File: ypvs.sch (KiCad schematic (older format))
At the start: 21 parts, among them J1 Servo, J2 LM_2596 _Input, J3 HV_Cable, J4 Motorcycle Battery, U1 Stm32f103_BluePill, U2 LM1117-3.3, U3 H11L1

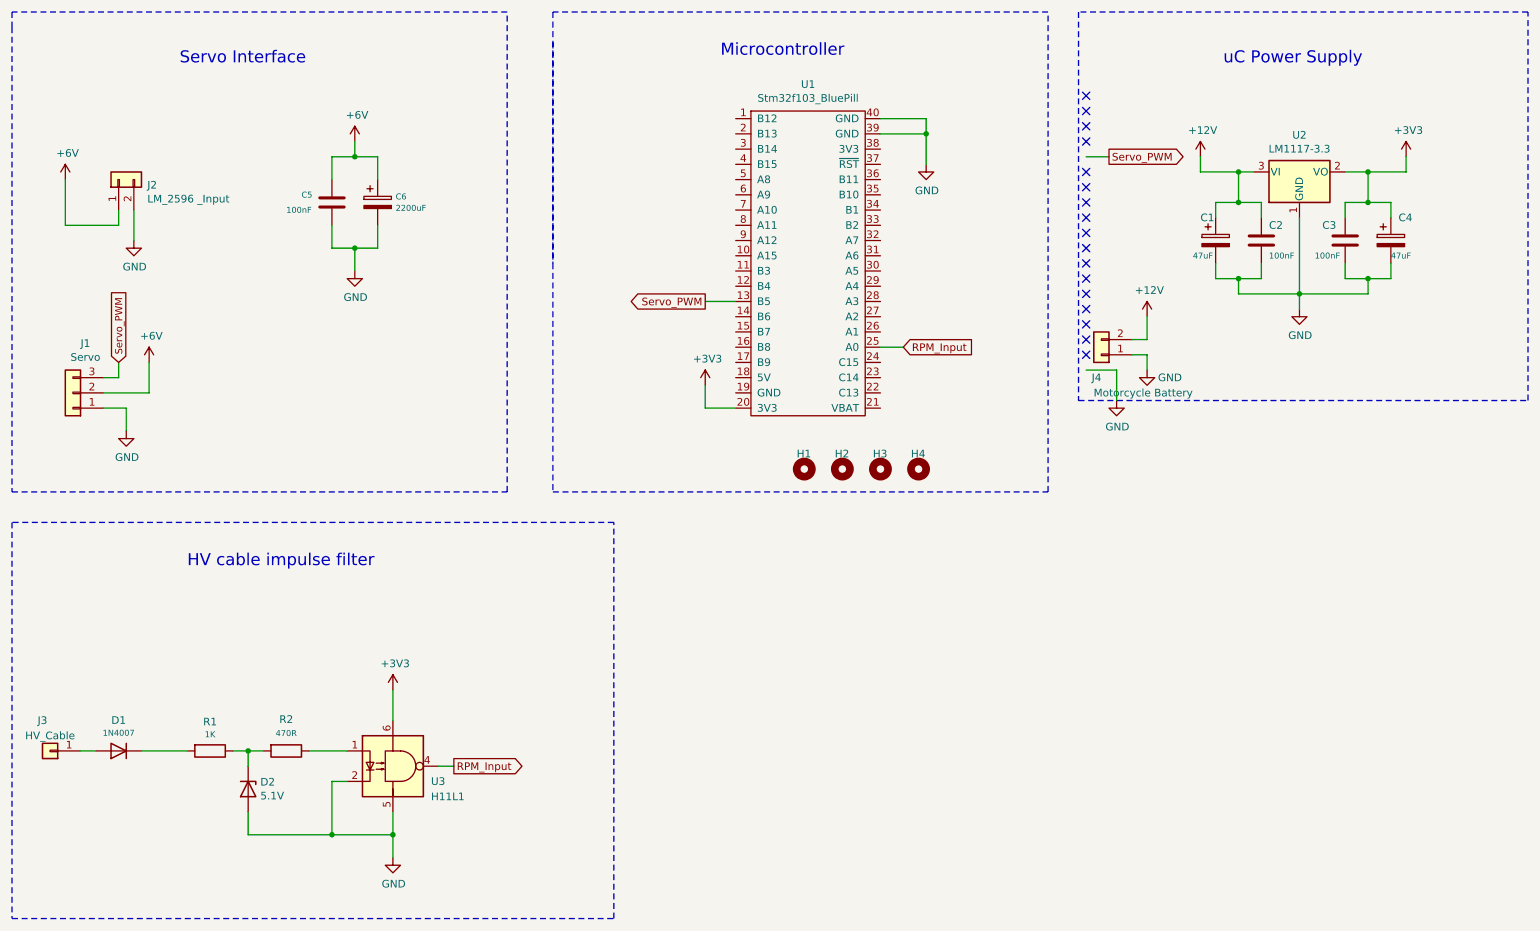
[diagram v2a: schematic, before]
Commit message: Added PCB traces
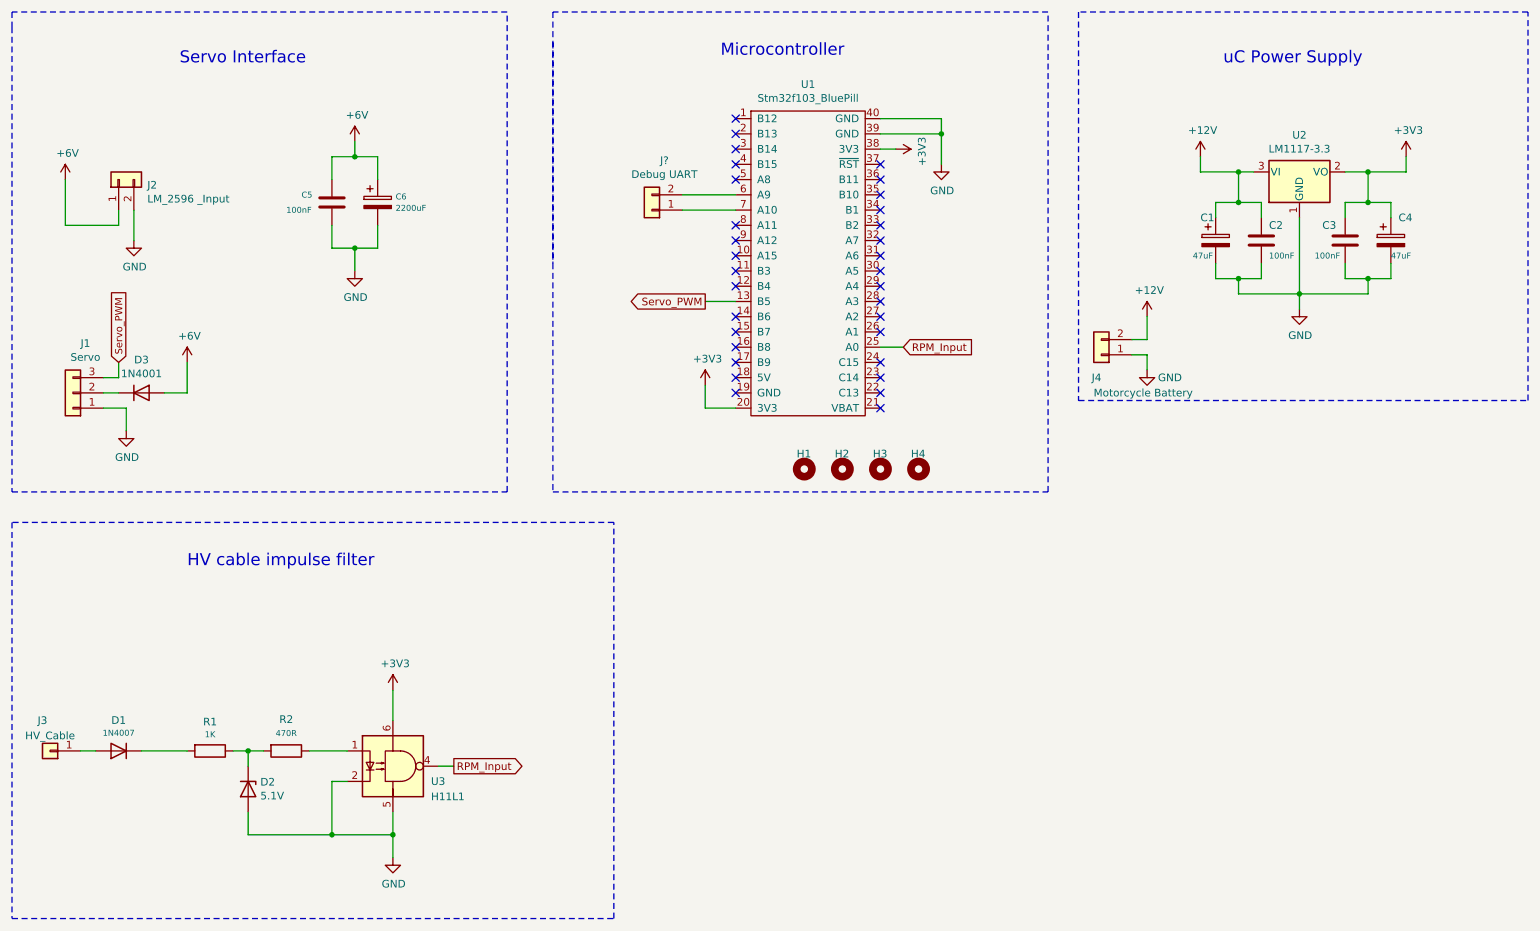
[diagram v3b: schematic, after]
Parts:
- added D3: 1N4001, symbol Device:D
- added J?: Debug UART, symbol Connector_Generic:Conn_01x02
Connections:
- net +3V3: now also U1.38 (3V3)
- net +6V: now also D3.2 (A); no longer J1.2 (Pin_2)
- net at U1.6 (A9): now also J?.2 (Pin_2)
- net at U1.7 (A10): now also J?.1 (Pin_1)
- new net: D3.1 (K), J1.2 (Pin_2)
- no-connect marks 17 -> 32
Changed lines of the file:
@@
 	9950 1700 9700 1700
 Connection ~ 9700 1700
-$Comp
-L power:GND #PWR09
-U 1 1 5F48A288
-P 8050 3200
-F 0 "#PWR09" H 8050 2950 50  0001 C CNN
-F 1 "GND" H 8055 3027 50  0000 C CNN
-F 2 "" H 8050 3200 50  0001 C CNN
-F 3 "" H 8050 3200 50  0001 C CNN
-	1    8050 3200
-	1    0    0    -1
-$EndComp
-Wire Wire Line
-	7850 3000 8050 3000
-Wire Wire Line
-	8050 3000 8050 3200
-Text GLabel 8000 1600 2    50   Output ~ 0
-Servo_PWM
-Wire Wire Line
-	7850 1600 8000 1600
 Wire Notes Line rgb(0, 0, 2)
 	7800 3200 10750 3200
@@
 Wire Notes Line rgb(0, 0, 2)
 	10750 650  7800 650
-Wire Notes Line rgb(0, 0, 2)
-	7800 650  7800 3200
 Text Notes 8750 1000 0    79   ~ 0
 uC Power Supply
@@
 Wire Notes Line rgb(0, 0, 2)
 	4350 650  4350 2300
-NoConn ~ 7850 2900
-NoConn ~ 7850 2800
-NoConn ~ 7850 2600
-NoConn ~ 7850 2500
-NoConn ~ 7850 2400
-NoConn ~ 7850 2300
-NoConn ~ 7850 2700
-NoConn ~ 7850 2200
-NoConn ~ 7850 2100
-NoConn ~ 7850 2000
-NoConn ~ 7850 1900
-NoConn ~ 7850 1800
-NoConn ~ 7850 1700
-NoConn ~ 7850 1500
-NoConn ~ 7850 1400
-NoConn ~ 7850 1300
-NoConn ~ 7850 1200
 Text Notes 5450 950  0    79   ~ 0
 Microcontroller
@@
 L power:+6V #PWR05
 U 1 1 5F4E2301
-P 1700 2950
-F 0 "#PWR05" H 1715 3215 50  0001 C CNN
-F 1 "+6V" H 1715 3123 50  0000 C CNN
-F 2 "" H 1700 2950 50  0001 C CNN
-F 3 "" H 1700 2950 50  0001 C CNN
-	1    1700 2950
-	1    0    0    -1
-$EndComp
-Wire Wire Line
-	1400 3150 1700 3150
-Wire Wire Line
-	1700 3150 1700 2950
+P 1950 2950
+F 0 "#PWR05" H 1965 3215 50  0001 C CNN
+F 1 "+6V" H 1965 3123 50  0000 C CNN
+F 2 "" H 1950 2950 50  0001 C CNN
+F 3 "" H 1950 2950 50  0001 C CNN
+	1    1950 2950
+	1    0    0    -1
+$EndComp
 Wire Notes Line rgb(0, 0, 8)
 	800  750  800  3800
@@
 Wire Wire Line
 	1250 5500 1350 5500
+Text GLabel 6650 2850 2    50   Input ~ 0
+RPM_Input
+Text GLabel 5350 2550 0    50   Output ~ 0
+Servo_PWM
+$Comp
+L power:+3V3 #PWR0101
+U 1 1 5F4A4007
+P 5350 3100
+F 0 "#PWR0101" H 5350 2950 50  0001 C CNN
+F 1 "+3V3" H 5365 3273 50  0000 C CNN
+F 2 "" H 5350 3100 50  0001 C CNN
+F 3 "" H 5350 3100 50  0001 C CNN
+	1    5350 3100
+	1    0    0    -1
+$EndComp
+$Comp
+L power:GND #PWR0102
+U 1 1 5F4A5041
+P 6900 1650
+F 0 "#PWR0102" H 6900 1400 50  0001 C CNN
+F 1 "GND" H 6905 1477 50  0000 C CNN
+F 2 "" H 6900 1650 50  0001 C CNN
+F 3 "" H 6900 1650 50  0001 C CNN
+	1    6900 1650
+	1    0    0    -1
+$EndComp
+Wire Wire Line
+	6650 2850 6500 2850
+Wire Wire Line
+	5550 2550 5350 2550
+$Comp
+L Mechanical:MountingHole H1
+U 1 1 5F4C806F
+P 6000 3650
+F 0 "H1" H 5950 3750 50  0000 L CNN
+F 1 "MountingHole" H 6100 3650 50  0001 L CNN
+F 2 "MountingHole:MountingHole_2.7mm_M2.5" H 6000 3650 50  0001 C CNN
+F 3 "~" H 6000 3650 50  0001 C CNN
+	1    6000 3650
+	1    0    0    -1
+$EndComp
+$Comp
+L Mechanical:MountingHole H2
+U 1 1 5F4C9D1D
+P 6250 3650
+F 0 "H2" H 6200 3750 50  0000 L CNN
+F 1 "MountingHole" H 6350 3650 50  0001 L CNN
+F 2 "MountingHole:MountingHole_2.7mm_M2.5" H 6250 3650 50  0001 C CNN
+F 3 "~" H 6250 3650 50  0001 C CNN
+	1    6250 3650
+	1    0    0    -1
+$EndComp
+$Comp
+L Mechanical:MountingHole H3
+U 1 1 5F4CA910
+P 6500 3650
+F 0 "H3" H 6450 3750 50  0000 L CNN
+F 1 "MountingHole" H 6600 3650 50  0001 L CNN
+F 2 "MountingHole:MountingHole_2.7mm_M2.5" H 6500 3650 50  0001 C CNN
+F 3 "~" H 6500 3650 50  0001 C CNN
+	1    6500 3650
+	1    0    0    -1
+$EndComp
+$Comp
+L Mechanical:MountingHole H4
+U 1 1 5F4CAE78
+P 6750 3650
+F 0 "H4" H 6700 3750 50  0000 L CNN
+F 1 "MountingHole" H 6850 3605 50  0001 L CNN
+F 2 "MountingHole:MountingHole_2.7mm_M2.5" H 6750 3650 50  0001 C CNN
+F 3 "~" H 6750 3650 50  0001 C CNN
+	1    6750 3650
+	1    0    0    -1
+$EndComp
+Wire Wire Line
+	5350 3100 5350 3250
+Wire Wire Line
+	5350 3250 5550 3250
+Wire Wire Line
+	6500 1450 6900 1450
+Wire Wire Line
+	6900 1450 6900 1650
+Wire Wire Line
+	6500 1350 6900 1350
+Wire Wire Line
+	6900 1350 6900 1450
+Connection ~ 6900 1450
+$Comp
+L power:+3V3 #PWR0103
+U 1 1 5F4B83B8
+P 6600 1550
+F 0 "#PWR0103" H 6600 1400 50  0001 C CNN
+F 1 "+3V3" H 6615 1723 50  0000 C CNN
+F 2 "" H 6600 1550 50  0001 C CNN
+F 3 "" H 6600 1550 50  0001 C CNN
+	1    6600 1550
+	0    1    1    0
+$EndComp
+Wire Wire Line
+	6500 1550 6600 1550
+Wire Notes Line rgb(0, 0, 2)
+	7800 650  7800 3200
+NoConn ~ 5550 1350
+NoConn ~ 5550 1450
+NoConn ~ 5550 1550
+NoConn ~ 5550 1650
+NoConn ~ 5550 1750
+NoConn ~ 5550 2050
+NoConn ~ 5550 2150
+NoConn ~ 5550 2250
+NoConn ~ 5550 2350
+NoConn ~ 5550 2450
+NoConn ~ 5550 2650
+NoConn ~ 5550 2750
+NoConn ~ 5550 2850
+NoConn ~ 5550 2950
+NoConn ~ 5550 3050
+NoConn ~ 5550 3150
+NoConn ~ 6500 3250
+NoConn ~ 6500 3150
+NoConn ~ 6500 3050
+NoConn ~ 6500 2950
+NoConn ~ 6500 2750
+NoConn ~ 6500 2650
+NoConn ~ 6500 2550
+NoConn ~ 6500 2450
+NoConn ~ 6500 2350
+NoConn ~ 6500 2250
+NoConn ~ 6500 2150
+NoConn ~ 6500 2050
+NoConn ~ 6500 1950
+NoConn ~ 6500 1850
+NoConn ~ 6500 1750
+NoConn ~ 6500 1650
+$Comp
+L Device:D D3
+U 1 1 5F51C076
+P 1650 3150
+F 0 "D3" H 1650 3367 50  0000 C CNN
+F 1 "1N4001" H 1650 3276 50  0000 C CNN
+F 2 "" H 1650 3150 50  0001 C CNN
+F 3 "~" H 1650 3150 50  0001 C CNN
+	1    1650 3150
+	1    0    0    -1
+$EndComp
+Wire Wire Line
+	1800 3150 1950 3150
+Wire Wire Line
+	1950 3150 1950 2950
+Wire Wire Line
+	1500 3150 1400 3150
+$Comp
+L Connector_Generic:Conn_01x02 J?
+U 1 1 5F521F21
+P 5000 1950
+F 0 "J?" H 4918 1625 50  0000 C CNN
+F 1 "Debug UART" H 4918 1716 50  0000 C CNN
+F 2 "" H 5000 1950 50  0001 C CNN
+F 3 "~" H 5000 1950 50  0001 C CNN
+	1    5000 1950
+	-1   0    0    1
+$EndComp
 $Comp
 L Ypvs:Stm32f103_BluePill U1
@@
 	1    0    0    -1
 $EndComp
-Text GLabel 6650 2850 2    50   Input ~ 0
-RPM_Input
-Text GLabel 5350 2550 0    50   Output ~ 0
-Servo_PWM
-$Comp
-L power:+3V3 #PWR0101
-U 1 1 5F4A4007
-P 5350 3100
-F 0 "#PWR0101" H 5350 2950 50  0001 C CNN
-F 1 "+3V3" H 5365 3273 50  0000 C CNN
-F 2 "" H 5350 3100 50  0001 C CNN
-F 3 "" H 5350 3100 50  0001 C CNN
-	1    5350 3100
-	1    0    0    -1
-$EndComp
-$Comp
-L power:GND #PWR0102
-U 1 1 5F4A5041
-P 6800 1650
-F 0 "#PWR0102" H 6800 1400 50  0001 C CNN
-F 1 "GND" H 6805 1477 50  0000 C CNN
-F 2 "" H 6800 1650 50  0001 C CNN
-F 3 "" H 6800 1650 50  0001 C CNN
-	1    6800 1650
-	1    0    0    -1
-$EndComp
-Wire Wire Line
-	6650 2850 6500 2850
-Wire Wire Line
-	5550 2550 5350 2550
-$Comp
-L Mechanical:MountingHole H1
-U 1 1 5F4C806F
-P 6000 3650
-F 0 "H1" H 5950 3750 50  0000 L CNN
-F 1 "MountingHole" H 6100 3650 50  0001 L CNN
-F 2 "MountingHole:MountingHole_2.7mm_M2.5" H 6000 3650 50  0001 C CNN
-F 3 "~" H 6000 3650 50  0001 C CNN
-	1    6000 3650
-	1    0    0    -1
-$EndComp
-$Comp
-L Mechanical:MountingHole H2
-U 1 1 5F4C9D1D
-P 6250 3650
-F 0 "H2" H 6200 3750 50  0000 L CNN
-F 1 "MountingHole" H 6350 3650 50  0001 L CNN
-F 2 "MountingHole:MountingHole_2.7mm_M2.5" H 6250 3650 50  0001 C CNN
-F 3 "~" H 6250 3650 50  0001 C CNN
-	1    6250 3650
-	1    0    0    -1
-$EndComp
-$Comp
-L Mechanical:MountingHole H3
-U 1 1 5F4CA910
-P 6500 3650
-F 0 "H3" H 6450 3750 50  0000 L CNN
-F 1 "MountingHole" H 6600 3650 50  0001 L CNN
-F 2 "MountingHole:MountingHole_2.7mm_M2.5" H 6500 3650 50  0001 C CNN
-F 3 "~" H 6500 3650 50  0001 C CNN
-	1    6500 3650
-	1    0    0    -1
-$EndComp
-$Comp
-L Mechanical:MountingHole H4
-U 1 1 5F4CAE78
-P 6750 3650
-F 0 "H4" H 6700 3750 50  0000 L CNN
-F 1 "MountingHole" H 6850 3605 50  0001 L CNN
-F 2 "MountingHole:MountingHole_2.7mm_M2.5" H 6750 3650 50  0001 C CNN
-F 3 "~" H 6750 3650 50  0001 C CNN
-	1    6750 3650
-	1    0    0    -1
-$EndComp
-Wire Wire Line
-	5350 3100 5350 3250
-Wire Wire Line
-	5350 3250 5550 3250
-Wire Wire Line
-	6500 1450 6800 1450
-Wire Wire Line
-	6800 1450 6800 1650
-Wire Wire Line
-	6500 1350 6800 1350
-Wire Wire Line
-	6800 1350 6800 1450
-Connection ~ 6800 1450
+Wire Wire Line
+	5200 1850 5550 1850
+Wire Wire Line
+	5200 1950 5550 1950
 $EndSCHEMATC

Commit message: Final v01
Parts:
- D3: footprint (none) -> Diode_THT:D_A-405_P7.62mm_Horizontal
- J5: renamed from J?; footprint (none) -> Connector_PinHeader_2.54mm:PinHeader_1x02_P2.54mm_Vertical
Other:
- moved on the sheet: C1, C2
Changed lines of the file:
@@
 $EndDescr
-$Comp
-L Regulator_Linear:LM1117-3.3 U2
-U 1 1 5F47817C
-P 9250 1700
-F 0 "U2" H 9250 1942 50  0000 C CNN
-F 1 "LM1117-3.3" H 9250 1851 50  0000 C CNN
-F 2 "Package_TO_SOT_SMD:SOT-223-3_TabPin2" H 9250 1700 50  0001 C CNN
-F 3 "http://www.ti.com/lit/ds/symlink/lm1117.pdf" H 9250 1700 50  0001 C CNN
-	1    9250 1700
-	1    0    0    -1
-$EndComp
 $Comp
 L power:GND #PWR01
@@
 $EndComp
 $Comp
-L Device:C C2
-U 1 1 5F47CC00
-P 9000 2150
-F 0 "C2" H 9050 2250 50  0000 L CNN
-F 1 "100nF" H 9050 2050 39  0000 L CNN
-F 2 "Capacitor_THT:C_Disc_D3.0mm_W1.6mm_P2.50mm" H 9038 2000 50  0001 C CNN
-F 3 "~" H 9000 2150 50  0001 C CNN
-	1    9000 2150
-	1    0    0    -1
-$EndComp
-$Comp
-L Device:CP C1
-U 1 1 5F47D5F7
-P 8700 2150
-F 0 "C1" H 8600 2300 50  0000 L CNN
-F 1 "47uF" H 8550 2050 39  0000 L CNN
-F 2 "Capacitor_THT:CP_Radial_D5.0mm_P2.00mm" H 8738 2000 50  0001 C CNN
-F 3 "~" H 8700 2150 50  0001 C CNN
-	1    8700 2150
-	1    0    0    -1
-$EndComp
-$Comp
 L Device:CP C4
 U 1 1 5F47E30A
@@
 Connection ~ 9700 1900
 Wire Wire Line
-	8950 1700 8850 1700
-Wire Wire Line
-	8850 1700 8850 1900
-Wire Wire Line
-	8850 1900 8700 1900
-Wire Wire Line
-	8700 1900 8700 2000
-Wire Wire Line
-	8850 1900 9000 1900
-Wire Wire Line
-	9000 1900 9000 2000
-Connection ~ 8850 1900
-Wire Wire Line
-	8700 2300 8700 2400
-Wire Wire Line
-	8700 2400 8850 2400
-Wire Wire Line
-	9000 2400 9000 2300
-Wire Wire Line
 	9550 2300 9550 2400
 Wire Wire Line
@@
 Wire Wire Line
 	9850 2400 9850 2300
-Wire Wire Line
-	8850 2400 8850 2500
-Wire Wire Line
-	8850 2500 9250 2500
-Connection ~ 8850 2400
-Wire Wire Line
-	8850 2400 9000 2400
 Connection ~ 9250 2500
 Wire Wire Line
@@
 L power:+12V #PWR010
 U 1 1 5F48516C
-P 8600 1600
-F 0 "#PWR010" H 8600 1450 50  0001 C CNN
-F 1 "+12V" H 8615 1773 50  0000 C CNN
-F 2 "" H 8600 1600 50  0001 C CNN
-F 3 "" H 8600 1600 50  0001 C CNN
-	1    8600 1600
+P 8450 1650
+F 0 "#PWR010" H 8450 1500 50  0001 C CNN
+F 1 "+12V" H 8465 1823 50  0000 C CNN
+F 2 "" H 8450 1650 50  0001 C CNN
+F 3 "" H 8450 1650 50  0001 C CNN
+	1    8450 1650
 	1    0    0    -1
 $EndComp
@@
 	1    0    0    -1
 $EndComp
-Wire Wire Line
-	8600 1600 8600 1700
-Wire Wire Line
-	8600 1700 8850 1700
-Connection ~ 8850 1700
 Wire Wire Line
 	9950 1600 9950 1700
@@
 L power:+12V #PWR014
 U 1 1 5F4C05D4
-P 8250 2650
-F 0 "#PWR014" H 8250 2500 50  0001 C CNN
-F 1 "+12V" H 8265 2823 50  0000 C CNN
-F 2 "" H 8250 2650 50  0001 C CNN
-F 3 "" H 8250 2650 50  0001 C CNN
-	1    8250 2650
+P 8250 2700
+F 0 "#PWR014" H 8250 2550 50  0001 C CNN
+F 1 "+12V" H 8265 2873 50  0000 C CNN
+F 2 "" H 8250 2700 50  0001 C CNN
+F 3 "" H 8250 2700 50  0001 C CNN
+	1    8250 2700
 	1    0    0    -1
 $EndComp
@@
 	8150 2800 8250 2800
 Wire Wire Line
-	8250 2800 8250 2650
+	8250 2800 8250 2700
 Wire Notes Line rgb(0, 0, 0)
 	800  6600 4750 6600
@@
 F 0 "D3" H 1650 3367 50  0000 C CNN
 F 1 "1N4001" H 1650 3276 50  0000 C CNN
-F 2 "" H 1650 3150 50  0001 C CNN
+F 2 "Diode_THT:D_A-405_P7.62mm_Horizontal" H 1650 3150 50  0001 C CNN
 F 3 "~" H 1650 3150 50  0001 C CNN
 	1    1650 3150
@@
 	1500 3150 1400 3150
 $Comp
-L Connector_Generic:Conn_01x02 J?
+L Connector_Generic:Conn_01x02 J5
 U 1 1 5F521F21
 P 5000 1950
-F 0 "J?" H 4918 1625 50  0000 C CNN
+F 0 "J5" H 4918 1625 50  0000 C CNN
 F 1 "Debug UART" H 4918 1716 50  0000 C CNN
-F 2 "" H 5000 1950 50  0001 C CNN
+F 2 "Connector_PinHeader_2.54mm:PinHeader_1x02_P2.54mm_Vertical" H 5000 1950 50  0001 C CNN
 F 3 "~" H 5000 1950 50  0001 C CNN
 	1    5000 1950
@@
 Wire Wire Line
 	5200 1950 5550 1950
+Wire Wire Line
+	8450 1650 8450 1700
+$Comp
+L Device:CP C1
+U 1 1 5F47D5F7
+P 8650 2150
+F 0 "C1" H 8550 2300 50  0000 L CNN
+F 1 "47uF" H 8500 2050 39  0000 L CNN
+F 2 "Capacitor_THT:CP_Radial_D5.0mm_P2.00mm" H 8688 2000 50  0001 C CNN
+F 3 "~" H 8650 2150 50  0001 C CNN
+	1    8650 2150
+	1    0    0    -1
+$EndComp
+$Comp
+L Device:C C2
+U 1 1 5F47CC00
+P 8950 2150
+F 0 "C2" H 9000 2250 50  0000 L CNN
+F 1 "100nF" H 9000 2050 39  0000 L CNN
+F 2 "Capacitor_THT:C_Disc_D3.0mm_W1.6mm_P2.50mm" H 8988 2000 50  0001 C CNN
+F 3 "~" H 8950 2150 50  0001 C CNN
+	1    8950 2150
+	1    0    0    -1
+$EndComp
+$Comp
+L Regulator_Linear:LM1117-3.3 U2
+U 1 1 5F47817C
+P 9250 1700
+F 0 "U2" H 9250 1942 50  0000 C CNN
+F 1 "LM1117-3.3" H 9250 1851 50  0000 C CNN
+F 2 "Package_TO_SOT_SMD:SOT-223-3_TabPin2" H 9250 1700 50  0001 C CNN
+F 3 "http://www.ti.com/lit/ds/symlink/lm1117.pdf" H 9250 1700 50  0001 C CNN
+	1    9250 1700
+	1    0    0    -1
+$EndComp
+Connection ~ 8250 2700
+Wire Wire Line
+	8250 2700 8250 2650
+Wire Wire Line
+	8650 2000 8650 1900
+Wire Wire Line
+	8650 1900 8800 1900
+Wire Wire Line
+	8950 1900 8950 2000
+Wire Wire Line
+	8800 1900 8800 1700
+Connection ~ 8800 1900
+Wire Wire Line
+	8800 1900 8950 1900
+Wire Wire Line
+	8650 2400 8650 2300
+Wire Wire Line
+	8950 2400 8950 2300
+Wire Wire Line
+	8650 2400 8800 2400
+Wire Wire Line
+	8800 2400 8800 2500
+Wire Wire Line
+	8800 2500 9250 2500
+Connection ~ 8800 2400
+Wire Wire Line
+	8800 2400 8950 2400
+Connection ~ 8800 1700
+Wire Wire Line
+	8800 1700 8450 1700
+Wire Wire Line
+	8800 1700 8950 1700
 $EndSCHEMATC
